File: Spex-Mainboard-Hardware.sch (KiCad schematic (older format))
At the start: 35 parts, among them P1 USB_OTG, P2 SWD Header, SW1 SW_PUSH, U2 NUP2201MR6, U4 NUP2201MR6, U5 NUP2201MR6, Y1 Crystal

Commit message: updated schematic
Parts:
- gave numbers to parts that had none: 13
- renumbered C10 to C7, C11 to C8, R9 to R12, R10 to R13, R6 to R7
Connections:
- net SPI0_SS is gone; now on net SPI0_CS: U6.1 (CATHODE)
- net SWD_CLK is gone; now on net PTB0: P2.4 (P4)
- net SWD_DIO is gone; now on net PTA7: P2.2 (P2)
- net Temp1: now also U3.9 (ADC0_DP0); no longer U3.26 (PTA4)
- net Temp2: now also U3.10 (ADC0_DM0); no longer U3.27 (PTA5)
- net Temp3: now reaches U3.11 (ADC0_DP3)
- net SD_Detect: now reaches U3.46 (PTC3)

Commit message: Schematics updated/components generated/PCB started
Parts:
- added C21: C, Capacitors_SMD:C_0603, symbol C
- added U14: AT45DB641E, SMD_Packages:SOIC-8-N, symbol AT45DB641E
- C1, C2, C3, C4, C5, C6, C7, C8: footprint (none) -> Capacitors_SMD:C_0603
- D1, D2, D3, D4: footprint (none) -> LEDs:LED_0603
- P1: footprint (none) -> Connect:USB_Micro-B
- P2: footprint (none) -> SPEX_Parts:SWD-10
- R1, R10, R11, R12, R13, R2, R3, R4, R5, R6, R7, R8, R9: footprint (none) -> Resistors_SMD:R_0603
- SW1: footprint (none) -> Buttons_Switches_SMD:SW_SPST_B3S-1000
- U1: footprint MODULE -> Housings_QFP:LQFP-32_7x7mm_Pitch0.8mm
- U2, U4, U5, U6: footprint MODULE -> SPEX_Parts:TSOP-6
- U3: footprint MODULE -> Housings_QFP:LQFP-64_10x10mm_Pitch0.5mm
- Y1: footprint (none) -> SPEX_Parts:CX3225GB16000D0HPQCC
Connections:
- net +3V3: now also C21.1, U14.6 (VCC)
- net GND: now also C21.2, U14.7 (GND)
- net SD_Detect: now also U3.45 (PTC2); no longer U3.46 (PTC3)
- net SPI0_CS: no longer U3.49 (PTC4)
- net SPI0_MISO: now also U14.8 (SO)
- net SPI0_MOSI: now also U14.1 (SI)
- net SPI0_SCK: now also U14.2 (SCK)
- net Relay2_ctrl: now reaches U3.35 (PTB0)
- net Relay1_ctrl: now reaches U3.36 (PTB1)
- net SD_CTRL: now reaches U3.44 (PTC1)
- new net SPI0_CS0: U3.49 (PTC4)
- new net SPI0_CS1: U14.4 (CS), U3.46 (PTC3)
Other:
- note added: "Flash Storage (64 Mbit)"
- moved on the sheet: C7, C8, D2, D3, D4, P2, R10, R11, R12, R13, R9, SW1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

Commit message: working on PCB layout
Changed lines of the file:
@@
 LIBS:Xicor
 LIBS:Zilog
+LIBS:KL03-QFN24
+LIBS:lt3652
+LIBS:lt4415
+LIBS:lt6105
+LIBS:mmqa
+LIBS:mos_n_numbered
+LIBS:MOS_P_NUM
+LIBS:ncp508
+LIBS:ncp1117st50t3g
+LIBS:npn-numbered
+LIBS:Power-cache
+LIBS:Power-rescue
+LIBS:si3407dv
+LIBS:tps563200
 LIBS:Spex-Mainboard-Hardware-cache
 EELAYER 25 0
@@
 $Descr A4 11693 8268
 encoding utf-8
-Sheet 1 4
+Sheet 1 7
 Title ""
 Date ""
@@
 $EndSheet
 $Sheet
-S 9700 3950 1400 1000
+S 9700 3550 1350 1250
 U 56DF75A2
 F0 "Power Distribution" 60
 F1 "SpexPowerBoard.sch" 60
-F2 "VBus" I L 9700 4000 60
-F3 "VBat" I L 9700 4100 60
-F4 "Bat1-2" I L 9700 4200 60
-F5 "Bat2-3" I L 9700 4300 60
-F6 "BatGnd" I L 9700 4400 60
-F7 "PowSDA" I L 9700 4500 60
-F8 "PowSCL" I L 9700 4600 60
-F9 "PowIRQ" I L 9700 4700 60
-F10 "3v3Out" I L 9700 4800 60
-F11 "3v3Gnd" I L 9700 4900 60
+F2 "VBus" I L 9700 3600 60
+F3 "VBat" I L 9700 3700 60
+F4 "Bat1-2" I L 9700 3800 60
+F5 "Bat2-3" I L 9700 3900 60
+F6 "BatGnd" I L 9700 4000 60
+F7 "PowSDA" I L 9700 4100 60
+F8 "PowSCL" I L 9700 4200 60
+F9 "PowIRQ" I L 9700 4300 60
+F10 "3v3Out" I L 9700 4400 60
+F11 "3v3Gnd" I L 9700 4500 60
+F12 "5vOut" I L 9700 4600 60
+F13 "5vGnd" I L 9700 4700 60
 $EndSheet
 $Comp
 L +3.3V #PWR019
 U 1 1 56DF91D1
-P 8950 4800
-F 0 "#PWR019" H 8950 4650 50  0001 C CNN
-F 1 "+3.3V" H 8950 4940 50  0000 C CNN
-F 2 "" H 8950 4800 60  0000 C CNN
-F 3 "" H 8950 4800 60  0000 C CNN
-	1    8950 4800
+P 8950 4400
+F 0 "#PWR019" H 8950 4250 50  0001 C CNN
+F 1 "+3.3V" H 8950 4540 50  0000 C CNN
+F 2 "" H 8950 4400 60  0000 C CNN
+F 3 "" H 8950 4400 60  0000 C CNN
+	1    8950 4400
 	1    0    0    -1
 $EndComp
@@
 L GND #PWR020
 U 1 1 56DF99D4
-P 8950 4900
-F 0 "#PWR020" H 8950 4650 50  0001 C CNN
-F 1 "GND" H 8950 4750 50  0000 C CNN
-F 2 "" H 8950 4900 60  0000 C CNN
-F 3 "" H 8950 4900 60  0000 C CNN
-	1    8950 4900
-	1    0    0    -1
-$EndComp
-Text GLabel 9550 4500 0    60   Input ~ 0
+P 8950 4500
+F 0 "#PWR020" H 8950 4250 50  0001 C CNN
+F 1 "GND" H 8950 4350 50  0000 C CNN
+F 2 "" H 8950 4500 60  0000 C CNN
+F 3 "" H 8950 4500 60  0000 C CNN
+	1    8950 4500
+	1    0    0    -1
+$EndComp
+Text GLabel 9550 4100 0    60   Input ~ 0
 I2C0_SDA
-Text GLabel 9550 4600 0    60   Input ~ 0
+Text GLabel 9550 4200 0    60   Input ~ 0
 I2C0_SCL
 Text GLabel 9550 5350 0    60   Input ~ 0
@@
 Text GLabel 6300 4000 2    60   Input ~ 0
 Relay2_ctrl
-Text GLabel 9550 4100 0    60   Input ~ 0
+Text GLabel 9550 3700 0    60   Input ~ 0
 VBatt
 Text GLabel 2650 7200 2    60   Input ~ 0
@@
 	8200 4650 8200 4750
 Wire Wire Line
-	8950 4900 9700 4900
-Wire Wire Line
-	8950 4800 9700 4800
+	8950 4500 9700 4500
+Wire Wire Line
+	8950 4400 9700 4400
 Wire Wire Line
 	9550 5350 9700 5350
@@
 	9700 5450 9550 5450
 Wire Wire Line
-	9550 4600 9700 4600
-Wire Wire Line
-	9700 4500 9550 4500
+	9550 4200 9700 4200
+Wire Wire Line
+	9700 4100 9550 4100
 Wire Wire Line
 	9550 5650 9700 5650
@@
 	2650 7200 2500 7200
 Wire Wire Line
-	9550 4100 9700 4100
+	9550 3700 9700 3700
 Wire Wire Line
 	4500 4200 4500 4500
@@
 Text Notes 4800 5250 0    60   ~ 0
 Flash Storage (64 Mbit)
+$Comp
+L +5V #PWR036
+U 1 1 56FE575C
+P 9500 4600
+F 0 "#PWR036" H 9500 4450 50  0001 C CNN
+F 1 "+5V" V 9518 4728 50  0000 L CNN
+F 2 "" H 9500 4600 50  0000 C CNN
+F 3 "" H 9500 4600 50  0000 C CNN
+	1    9500 4600
+	0    -1   -1   0
+$EndComp
+$Comp
+L GND #PWR037
+U 1 1 56FE5B17
+P 9500 4750
+F 0 "#PWR037" H 9500 4500 50  0001 C CNN
+F 1 "GND" H 9508 4577 50  0000 C CNN
+F 2 "" H 9500 4750 50  0000 C CNN
+F 3 "" H 9500 4750 50  0000 C CNN
+	1    9500 4750
+	1    0    0    -1
+$EndComp
+Wire Wire Line
+	9700 4600 9500 4600
+Wire Wire Line
+	9700 4700 9500 4700
+Wire Wire Line
+	9500 4700 9500 4750
+$Comp
+L GND #PWR038
+U 1 1 56FE600A
+P 9550 4000
+F 0 "#PWR038" H 9550 3750 50  0001 C CNN
+F 1 "GND" V 9558 3872 50  0000 R CNN
+F 2 "" H 9550 4000 50  0000 C CNN
+F 3 "" H 9550 4000 50  0000 C CNN
+	1    9550 4000
+	0    1    1    0
+$EndComp
+Wire Wire Line
+	9700 4000 9550 4000
 $EndSCHEMATC

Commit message: schematic updated
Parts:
- removed C7, C8: C, Capacitors_SMD:C_0603, symbol C
- R1: value R -> 1K
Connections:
- net SPI0_CS is gone; now on net SPI0_CS0: U6.1 (CATHODE)
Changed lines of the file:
@@
 LIBS:valves
 LIBS:parts
-LIBS:PRESSURE-BMP180_LGA7_
 LIBS:74xgxx
 LIBS:ac-dc
@@
 $EndComp
 $Comp
-L GND #PWR04
-U 1 1 5657DEDB
-P 5150 4850
-F 0 "#PWR04" H 5150 4600 50  0001 C CNN
-F 1 "GND" H 5150 4700 50  0000 C CNN
-F 2 "" H 5150 4850 60  0000 C CNN
-F 3 "" H 5150 4850 60  0000 C CNN
-	1    5150 4850
-	1    0    0    -1
-$EndComp
-$Comp
 L C C2
 U 1 1 5657EA4F
@@
 $EndComp
 $Comp
-L C C7
-U 1 1 5679E0BF
-P 4750 4650
-F 0 "C7" H 4775 4750 50  0000 L CNN
-F 1 "C" H 4775 4550 50  0000 L CNN
-F 2 "Capacitors_SMD:C_0603" H 4788 4500 30  0001 C CNN
-F 3 "" H 4750 4650 60  0000 C CNN
-	1    4750 4650
-	1    0    0    -1
-$EndComp
-$Comp
-L C C8
-U 1 1 5679E124
-P 5500 4650
-F 0 "C8" H 5525 4750 50  0000 L CNN
-F 1 "C" H 5525 4550 50  0000 L CNN
-F 2 "Capacitors_SMD:C_0603" H 5538 4500 30  0001 C CNN
-F 3 "" H 5500 4650 60  0000 C CNN
-	1    5500 4650
-	1    0    0    -1
-$EndComp
-$Comp
 L GND #PWR012
 U 1 1 5679E224
@@
 P 2200 2300
 F 0 "R1" V 2280 2300 50  0000 C CNN
-F 1 "R" V 2200 2300 50  0000 C CNN
+F 1 "1K" V 2200 2300 50  0000 C CNN
 F 2 "Resistors_SMD:R_0603" V 2130 2300 30  0001 C CNN
 F 3 "" H 2200 2300 30  0000 C CNN
@@
 SPI0_MOSI
 Text GLabel 9550 2000 0    60   Input ~ 0
-SPI0_CS
+SPI0_CS0
 Text Notes 9600 650  0    60   ~ 0
 Data Bus Protection\n
@@
 Wire Wire Line
 	4500 4500 5000 4500
-Connection ~ 4750 4500
 Wire Wire Line
 	5300 4500 5800 4500
-Connection ~ 5500 4500
-Wire Wire Line
-	4750 4800 5500 4800
-Wire Wire Line
-	5150 4850 5150 4800
-Connection ~ 5150 4800
 Wire Wire Line
 	2200 2500 2800 2500

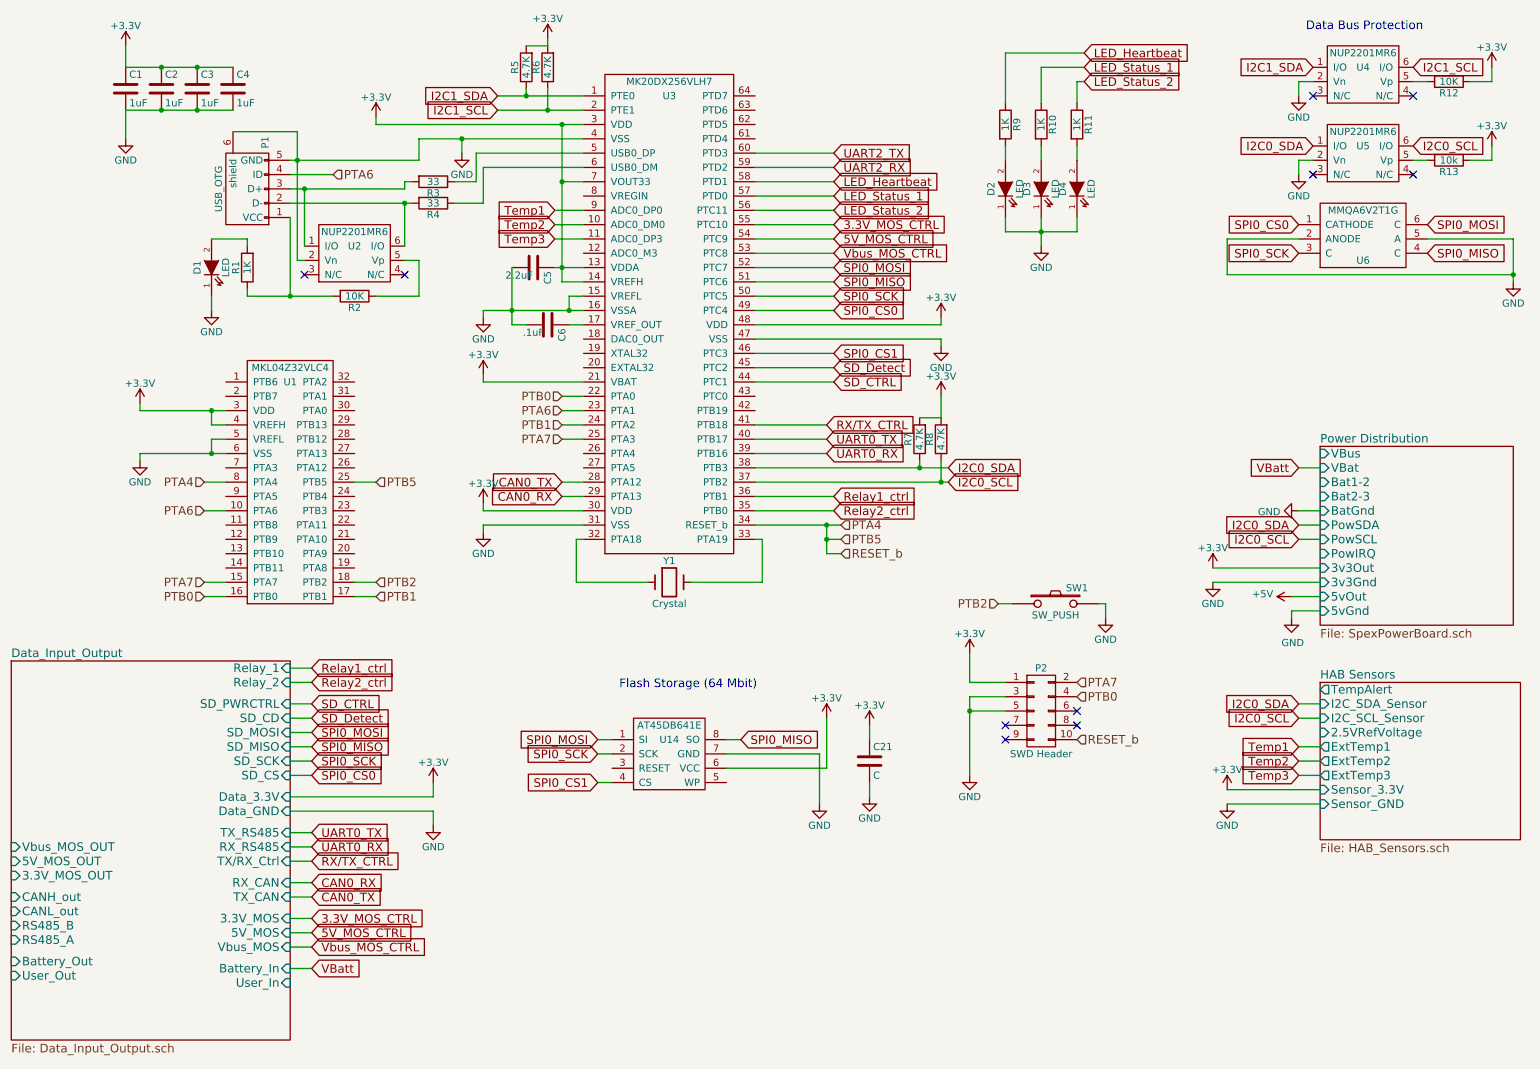
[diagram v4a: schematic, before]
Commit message: continued PCB layout, small schematic changes
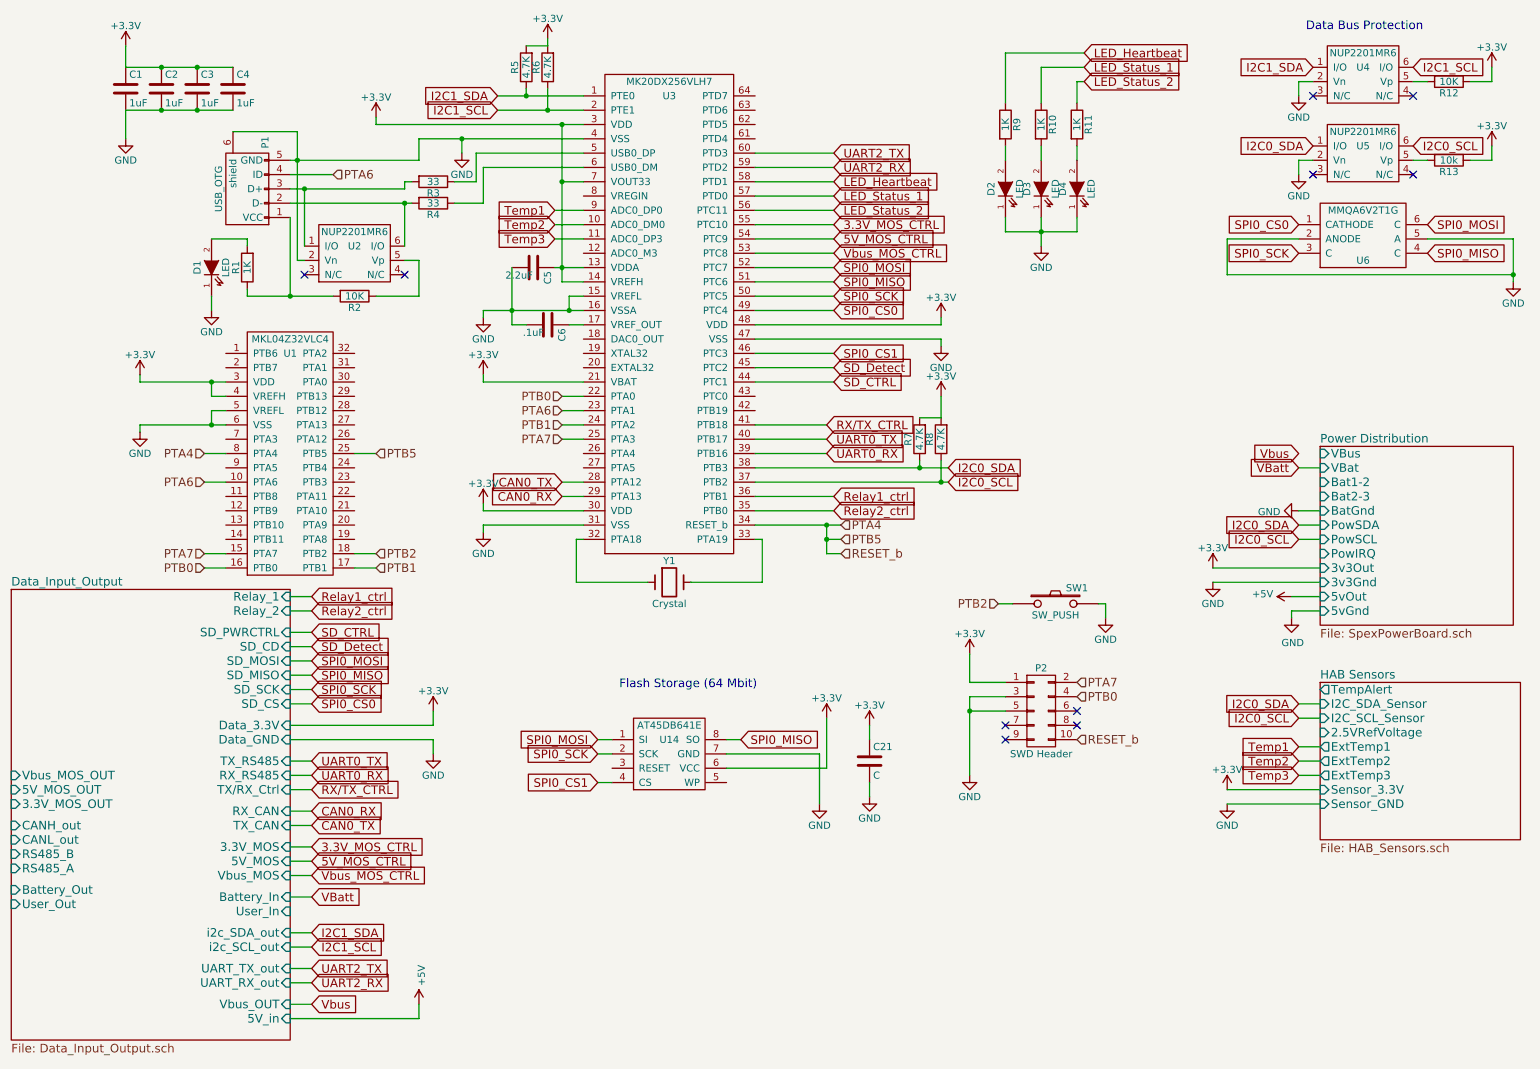
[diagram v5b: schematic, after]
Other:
- moved on the sheet: U1

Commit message: updated board
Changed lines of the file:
@@
 LIBS:valves
 LIBS:parts
+LIBS:PRESSURE-BMP180_LGA7_
 LIBS:74xgxx
 LIBS:ac-dc
@@
 Wire Wire Line
 	2650 7450 2500 7450
+Wire Wire Line
+	9550 3600 9700 3600
 $EndSCHEMATC

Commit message: board layout 95% complete
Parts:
- added R18: 10K, Resistors_SMD:R_0603, symbol R
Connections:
- net +3V3: now also U14.5 (WP), R18.1
- net Flash_Reset: now reaches U3.43 (PTC0)
- net Flash_Reset: now also U14.3 (RESET), R18.2
- net PTA4 renamed RESET_b
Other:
- moved on the sheet: C21, U14
